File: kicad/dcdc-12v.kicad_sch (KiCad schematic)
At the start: 12 parts, among them U2 XL7005A

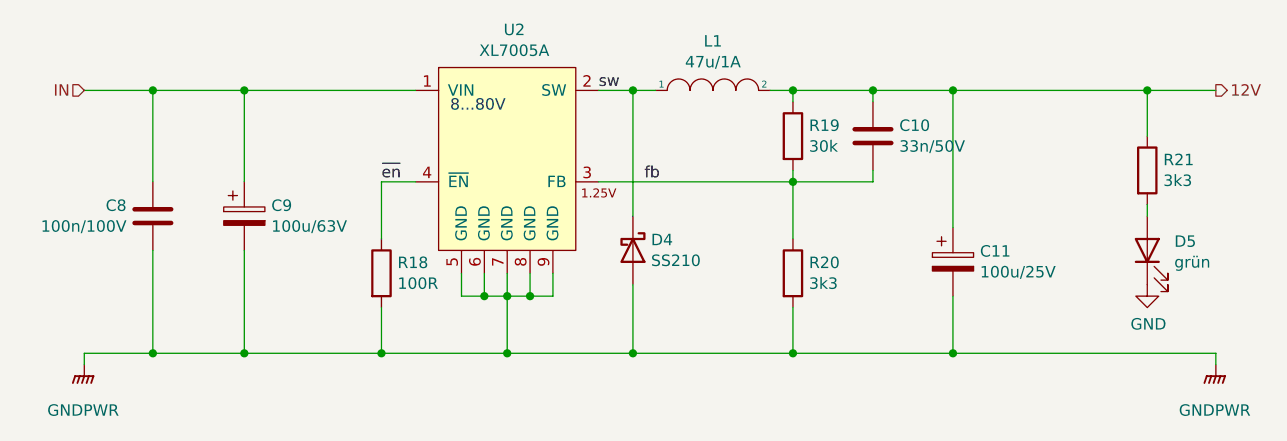
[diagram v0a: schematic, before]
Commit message: created bom for order lcsc
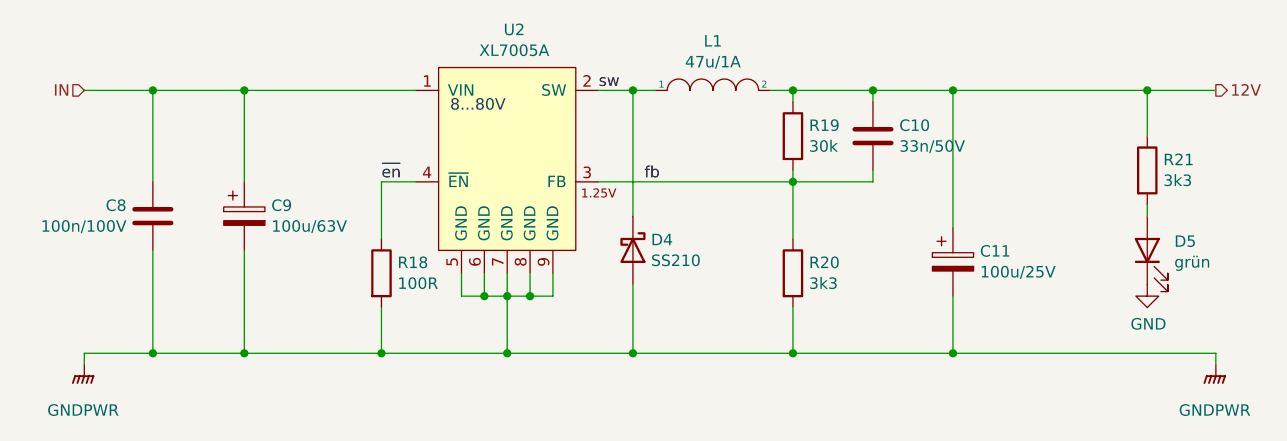
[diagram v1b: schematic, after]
